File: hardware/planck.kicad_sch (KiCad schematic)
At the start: 97 parts, among them SW1 SW_Push, SW10 SW_Push, SW11 SW_Push, SW12 SW_Push, SW13 SW_Push, SW14 SW_Push, SW15 SW_Push, SW16 SW_Push, SW17 SW_Push, SW18 SW_Push, SW19 SW_Push, SW2 SW_Push, SW20 SW_Push, SW21 SW_Push, SW22 SW_Push, SW23 SW_Push, SW24 SW_Push, SW25 SW_Push, SW26 SW_Push, SW27 SW_Push, SW28 SW_Push, SW29 SW_Push, SW3 SW_Push, SW30 SW_Push, SW31 SW_Push, SW32 SW_Push, SW33 SW_Push, SW34 SW_Push, SW35 SW_Push, SW36 SW_Push, SW37 SW_Push, SW38 SW_Push, SW39 SW_Push, SW4 SW_Push, SW40 SW_Push, SW41 SW_Push, SW42 SW_Push, SW43 SW_Push, SW44 SW_Push, SW45 SW_Push, SW46 SW_Push, SW47 SW_Push, SW48 SW_Push, SW5 SW_Push, SW6 SW_Push, SW7 SW_Push, SW8 SW_Push, SW9 SW_Push, U1 STM32F103CBTx

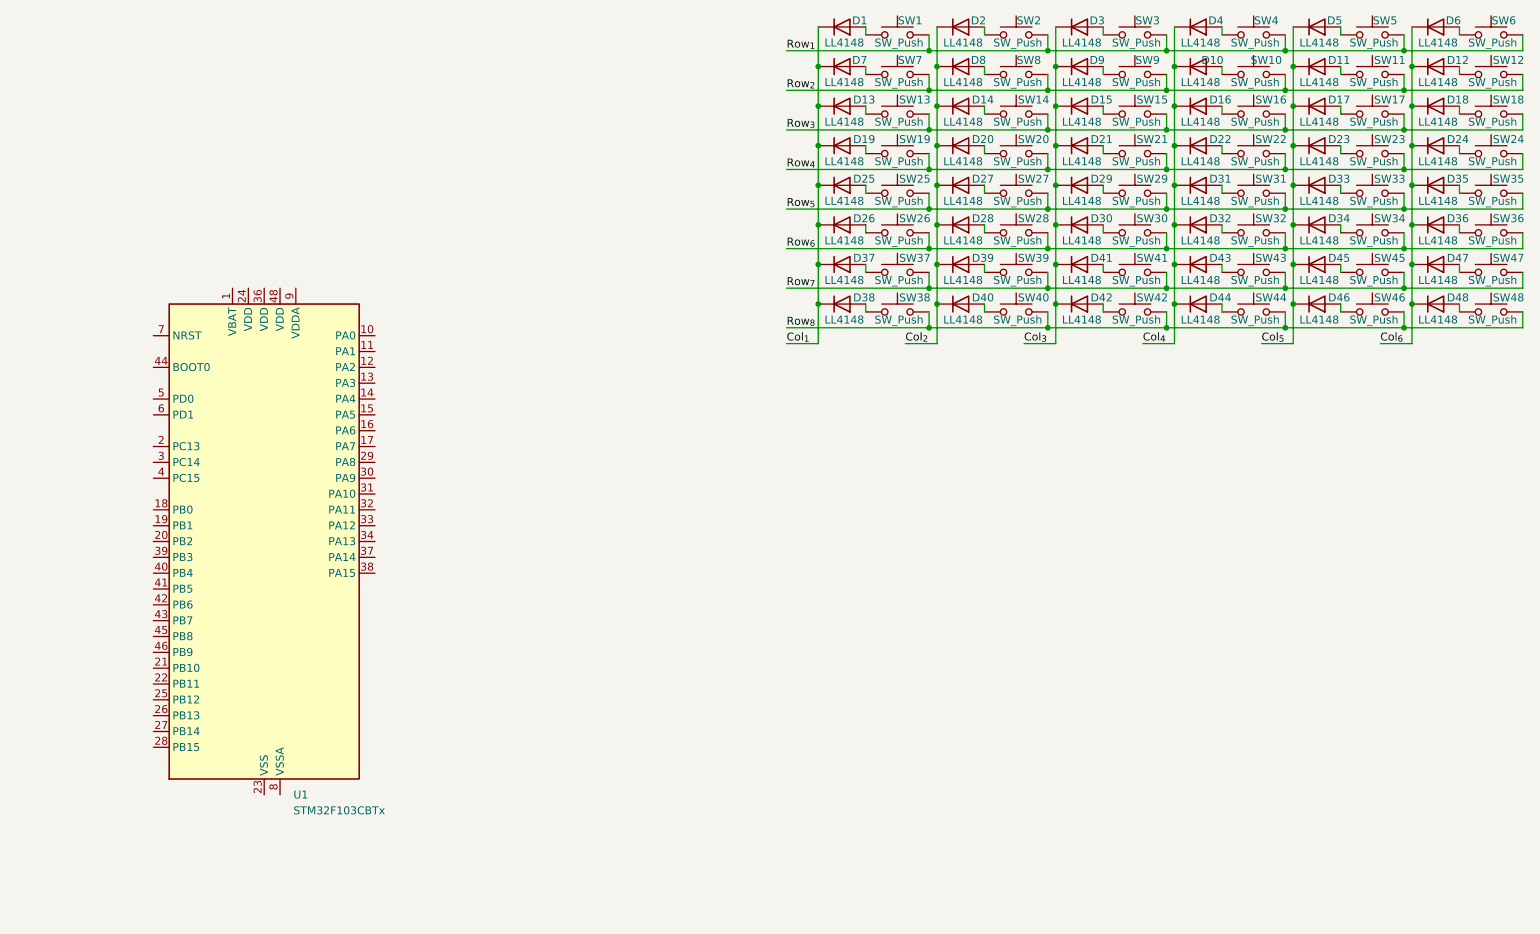
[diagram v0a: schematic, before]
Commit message: 添加几个元件
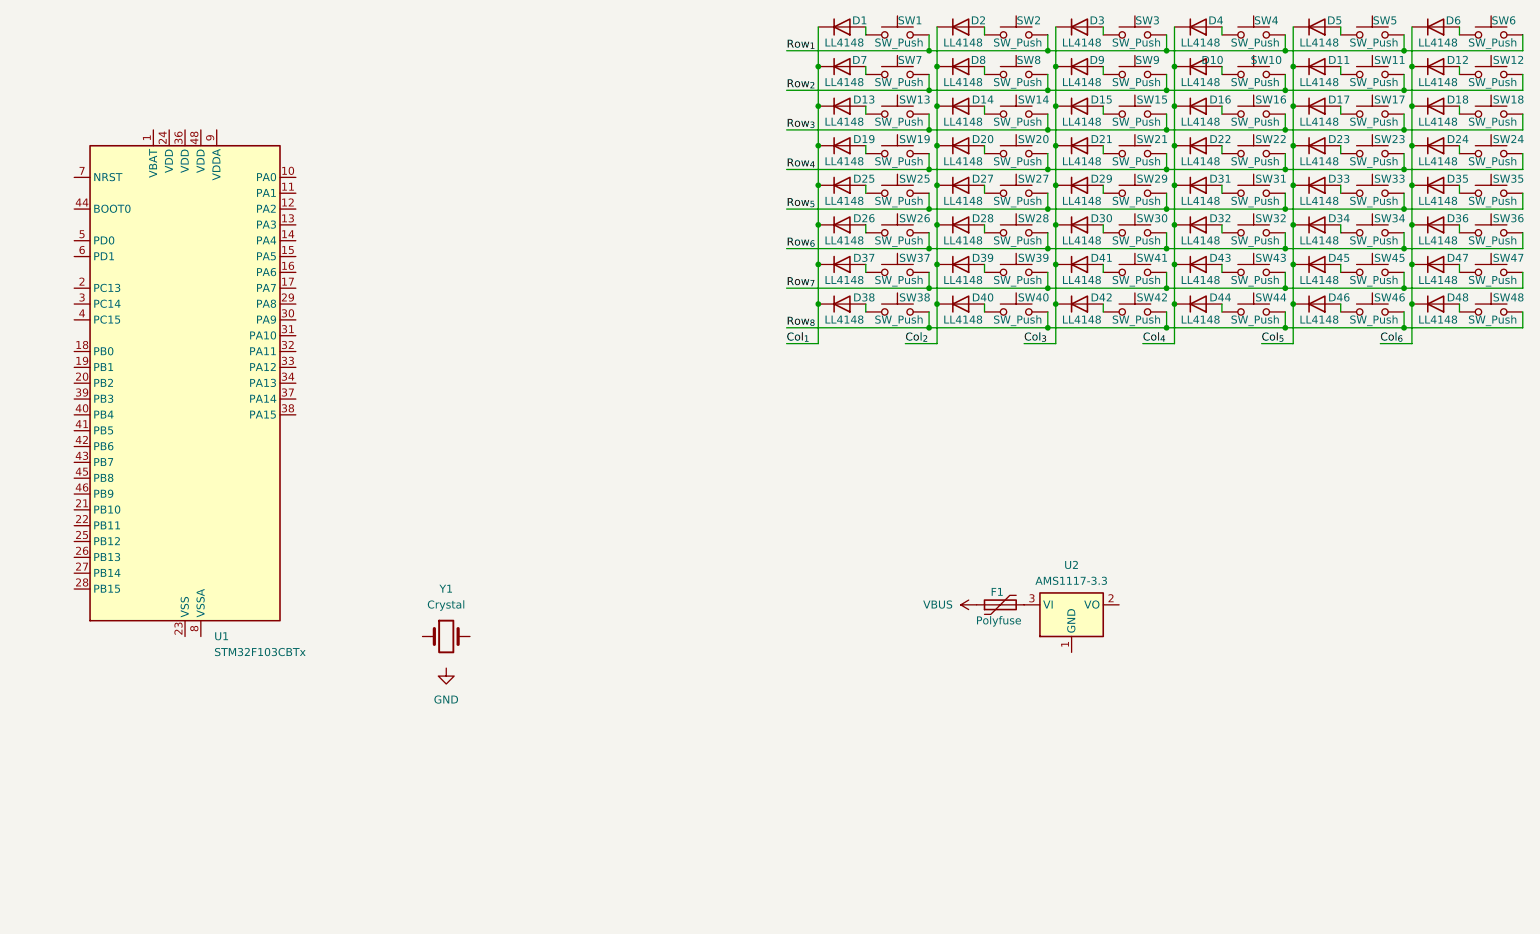
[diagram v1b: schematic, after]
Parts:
- added F1: Polyfuse, symbol Device:Polyfuse
- added U2: AMS1117-3.3, Package_TO_SOT_SMD:SOT-223-3_TabPin2, symbol Regulator_Linear:AMS1117-3.3
- added Y1: Crystal, symbol Device:Crystal
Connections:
- new net: F1.2, U2.3 (VI)
- new net VBUS: F1.1
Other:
- moved on the sheet: U1

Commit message: feat: 电源第一版
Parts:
- added J1: USB_C_Receptacle_USB2.0_16P, symbol Connector:USB_C_Receptacle_USB2.0_16P
- added R1, R2: 512, symbol Device:R
- added R3: 152, symbol Device:R
- added U3: USBLC6-2P6, Package_TO_SOT_SMD:SOT-666, symbol Power_Protection:USBLC6-2P6
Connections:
- net at U2.1 (GND): now also J1.A1 (GND), J1.A12 (GND), J1.B1 (GND), J1.B12 (GND), J1.S1 (SHIELD), U3.2 (GND)
- net at U2.2 (VO): now also R3.2
- net VBUS: no longer names the net of F1.1
- net VBUS: now also J1.A4 (VBUS), J1.A9 (VBUS), J1.B4 (VBUS), J1.B9 (VBUS), U3.5 (VBUS)
- new net: J1.A7 (D-), J1.B7 (D-), U3.1 (I/O1)
- new net: J1.A6 (D+), J1.B6 (D+), U3.3 (I/O2)
- new net: J1.A5 (CC1), R1.1
- new net: R1.2, R2.2
- new net: J1.B5 (CC2), R2.1
- new net D+: R3.1, U3.4 (I/O2)
- new net D-: U3.6 (I/O1)
- no-connect marks 0 -> 3
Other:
- moved on the sheet: F1, U2

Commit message: feat: 晶振
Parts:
- added C1, C2: 220, symbol Device:C
- Y1: value Crystal -> 12M
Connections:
- net GND: now also J1.A1 (GND), J1.A12 (GND), J1.B1 (GND), J1.B12 (GND), J1.S1 (SHIELD), U1.23 (VSS), U1.35 (VSS), U1.47 (VSS), U1.8 (VSSA), U2.1 (GND), U3.2 (GND), C1.2, C2.2
- net +3V3: now reaches R3.2, U2.2 (VO)
- net +3V3: now also U1.1 (VBAT), U1.24 (VDD), U1.36 (VDD), U1.48 (VDD), U1.9 (VDDA)
- net OSC_IN: now reaches U1.5 (PD0)
- net OSC_IN: now also Y1.2, C2.1
- net OSC_OUT: now reaches U1.6 (PD1)
- net OSC_OUT: now also Y1.1, C1.1
- no-connect marks 3 -> 2
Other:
- moved on the sheet: F1, J1, R1, R2, R3, U2, U3, Y1
